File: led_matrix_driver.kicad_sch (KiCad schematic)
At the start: 29 parts, among them J2 Screw_Terminal_01x02, J3 Screw_Terminal_01x02, J4 Conn_01x06_Pin, J5 Conn_02x17_Odd_Even, SW1 CK KMS221GPLFS, SW2 CK KMS221GPLFS, U2 Pico, U3 ESP32-WROOM-32, U4 AP1117-33, U5 74HCT245, U6 Teensy4.0, U7 74HCT245

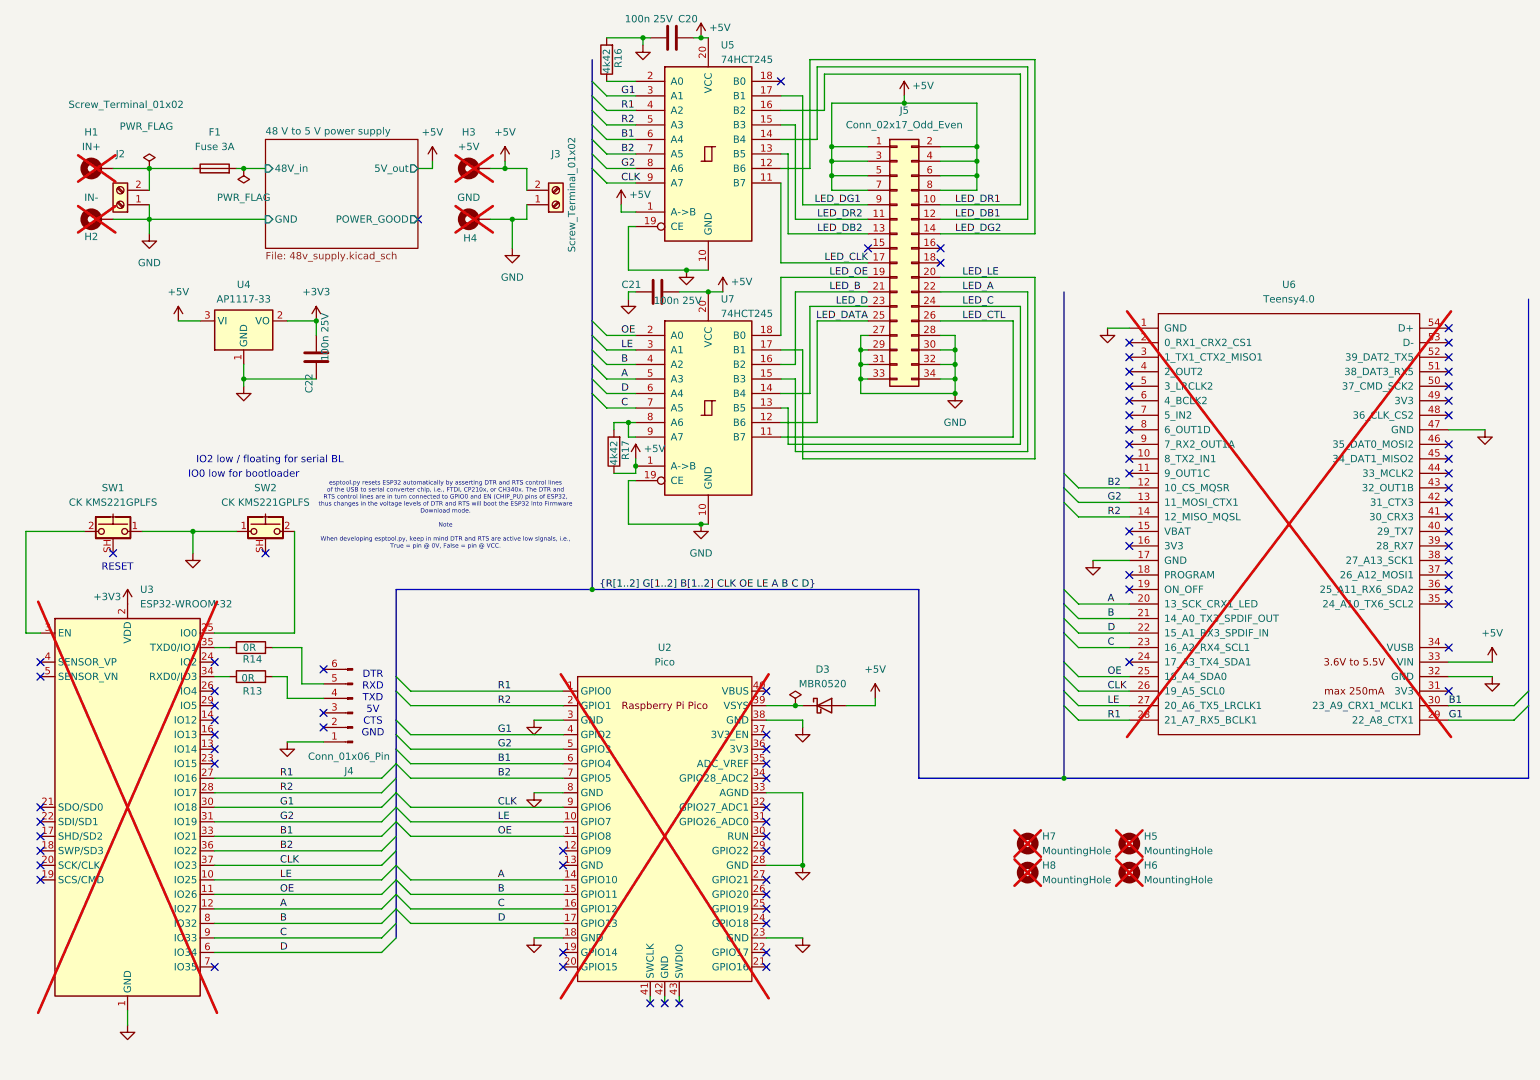
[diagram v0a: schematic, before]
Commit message: Added SPI ESP32-Pico. Last component JLCPCB codes
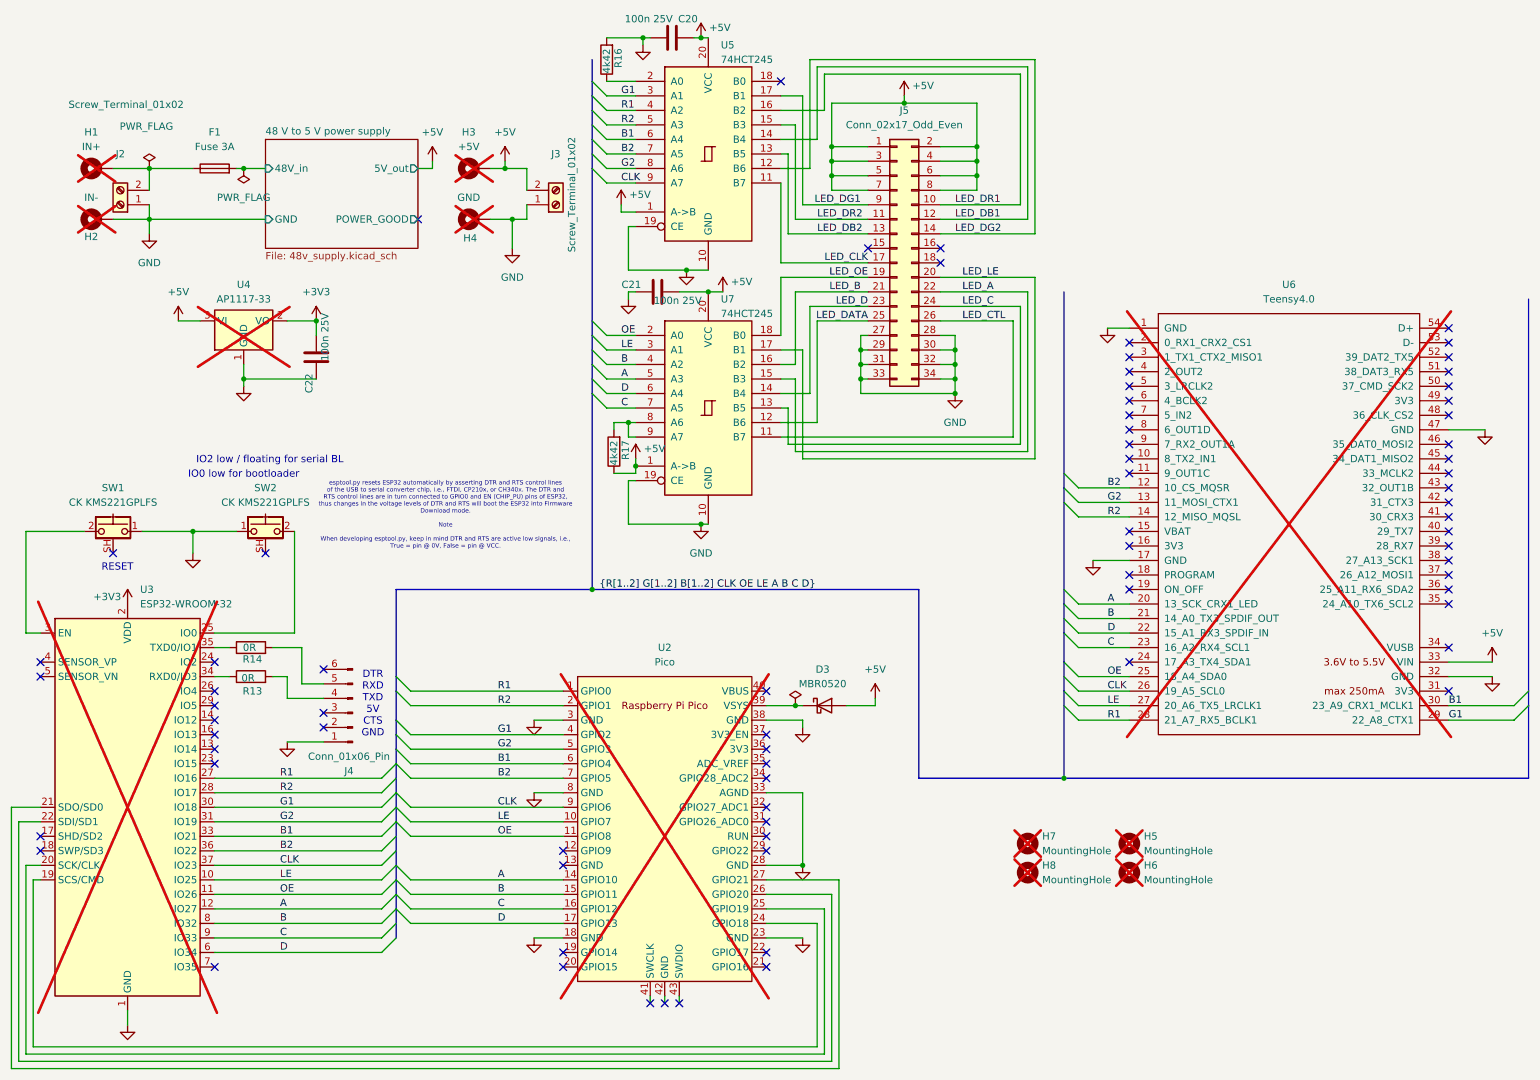
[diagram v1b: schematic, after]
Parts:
- R16, R17: LCSC (none) -> C2933223
- U4: now not fitted
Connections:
- net at U2.24 (GPIO18): now also U3.19 (SCS/CMD)
- net at U2.25 (GPIO19): now also U3.20 (SCK/CLK)
- net at U2.26 (GPIO20): now also U3.22 (SDI/SD1)
- net at U2.27 (GPIO21): now also U3.21 (SDO/SD0)
- no-connect marks 84 -> 76
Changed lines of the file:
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@@
 	)
 	(no_connect
-		(at 144.78 171.45)
-	)
-	(no_connect
 		(at 109.22 176.53)
 	)
@@
 	)
 	(no_connect
-		(at 17.78 163.83)
-	)
-	(no_connect
 		(at 67.31 137.16)
 	)
@@
 	)
 	(no_connect
-		(at 144.78 163.83)
-	)
-	(no_connect
 		(at 48.26 140.97)
 	)
@@
 	)
 	(no_connect
-		(at 17.78 161.29)
-	)
-	(no_connect
 		(at 30.48 106.68)
 	)
@@
 	)
 	(no_connect
-		(at 144.78 168.91)
-	)
-	(no_connect
 		(at 264.16 82.55)
 	)
@@
 	)
 	(no_connect
-		(at 17.78 153.67)
-	)
-	(no_connect
 		(at 129.54 185.42)
 	)
@@
 	)
 	(no_connect
-		(at 144.78 166.37)
-	)
-	(no_connect
 		(at 144.78 156.21)
 	)
@@
 	)
 	(no_connect
-		(at 17.78 151.13)
-	)
-	(no_connect
 		(at 208.28 92.71)
 	)
@@
 	(wire
 		(pts
+			(xy 17.78 153.67) (xy 13.97 153.67)
+		)
+		(stroke
+			(width 0)
+			(type default)
+		)
+	)
+	(wire
+		(pts
 			(xy 168.91 26.67) (xy 168.91 27.94)
 		)
@@
 	(wire
 		(pts
+			(xy 154.94 194.31) (xy 15.24 194.31)
+		)
+		(stroke
+			(width 0)
+			(type default)
+		)
+	)
+	(wire
+		(pts
 			(xy 102.87 45.72) (xy 102.87 48.26)
 		)
@@
 	(wire
 		(pts
+			(xy 154.94 168.91) (xy 154.94 194.31)
+		)
+		(stroke
+			(width 0)
+			(type default)
+		)
+	)
+	(wire
+		(pts
 			(xy 48.26 146.05) (xy 77.47 146.05)
 		)
@@
 	(wire
 		(pts
+			(xy 153.67 171.45) (xy 153.67 193.04)
+		)
+		(stroke
+			(width 0)
+			(type default)
+		)
+	)
+	(wire
+		(pts
 			(xy 175.26 68.58) (xy 177.8 68.58)
 		)
@@
 		)
 	)
+	(wire
+		(pts
+			(xy 144.78 171.45) (xy 153.67 171.45)
+		)
+		(stroke
+			(width 0)
+			(type default)
+		)
+	)
 	(bus
 		(pts
@@
 	(wire
 		(pts
+			(xy 12.7 196.85) (xy 12.7 151.13)
+		)
+		(stroke
+			(width 0)
+			(type default)
+		)
+	)
+	(wire
+		(pts
 			(xy 66.04 66.04) (xy 66.04 68.58)
 		)
@@
 	(wire
 		(pts
+			(xy 16.51 163.83) (xy 16.51 193.04)
+		)
+		(stroke
+			(width 0)
+			(type default)
+		)
+	)
+	(wire
+		(pts
 			(xy 151.13 148.59) (xy 151.13 161.29)
 		)
@@
 	(wire
 		(pts
+			(xy 17.78 163.83) (xy 16.51 163.83)
+		)
+		(stroke
+			(width 0)
+			(type default)
+		)
+	)
+	(wire
+		(pts
 			(xy 118.11 83.82) (xy 118.11 85.09)
 		)
@@
 	(wire
 		(pts
+			(xy 13.97 153.67) (xy 13.97 195.58)
+		)
+		(stroke
+			(width 0)
+			(type default)
+		)
+	)
+	(wire
+		(pts
 			(xy 30.48 48.26) (xy 36.83 48.26)
 		)
@@
 	(wire
 		(pts
+			(xy 144.78 168.91) (xy 154.94 168.91)
+		)
+		(stroke
+			(width 0)
+			(type default)
+		)
+	)
+	(wire
+		(pts
 			(xy 151.13 26.67) (xy 151.13 45.72)
 		)
@@
 	(wire
 		(pts
+			(xy 15.24 161.29) (xy 17.78 161.29)
+		)
+		(stroke
+			(width 0)
+			(type default)
+		)
+	)
+	(wire
+		(pts
 			(xy 156.21 35.56) (xy 162.56 35.56)
 		)
@@
 	(wire
 		(pts
+			(xy 15.24 194.31) (xy 15.24 161.29)
+		)
+		(stroke
+			(width 0)
+			(type default)
+		)
+	)
+	(wire
+		(pts
 			(xy 181.61 35.56) (xy 181.61 38.1)
 		)
@@
 	(wire
 		(pts
+			(xy 157.48 196.85) (xy 12.7 196.85)
+		)
+		(stroke
+			(width 0)
+			(type default)
+		)
+	)
+	(wire
+		(pts
 			(xy 199.39 95.25) (xy 208.28 95.25)
 		)
@@
 	(wire
 		(pts
+			(xy 13.97 195.58) (xy 156.21 195.58)
+		)
+		(stroke
+			(width 0)
+			(type default)
+		)
+	)
+	(wire
+		(pts
 			(xy 82.55 156.21) (xy 109.22 156.21)
 		)
@@
 	(wire
 		(pts
+			(xy 16.51 193.04) (xy 153.67 193.04)
+		)
+		(stroke
+			(width 0)
+			(type default)
+		)
+	)
+	(wire
+		(pts
 			(xy 82.55 138.43) (xy 109.22 138.43)
 		)
@@
 		)
 	)
+	(wire
+		(pts
+			(xy 12.7 151.13) (xy 17.78 151.13)
+		)
+		(stroke
+			(width 0)
+			(type default)
+		)
+	)
 	(bus
 		(pts
@@
 	(wire
 		(pts
+			(xy 144.78 163.83) (xy 157.48 163.83)
+		)
+		(stroke
+			(width 0)
+			(type default)
+		)
+	)
+	(wire
+		(pts
 			(xy 199.39 130.81) (xy 208.28 130.81)
 		)
@@
 	(wire
 		(pts
+			(xy 144.78 166.37) (xy 156.21 166.37)
+		)
+		(stroke
+			(width 0)
+			(type default)
+		)
+	)
+	(wire
+		(pts
 			(xy 199.39 120.65) (xy 208.28 120.65)
 		)
@@
 	(wire
 		(pts
+			(xy 157.48 163.83) (xy 157.48 196.85)
+		)
+		(stroke
+			(width 0)
+			(type default)
+		)
+	)
+	(wire
+		(pts
 			(xy 144.78 173.99) (xy 151.13 173.99)
 		)
@@
 	(wire
 		(pts
+			(xy 156.21 166.37) (xy 156.21 195.58)
+		)
+		(stroke
+			(width 0)
+			(type default)
+		)
+	)
+	(wire
+		(pts
 			(xy 53.34 39.37) (xy 57.15 39.37)
 		)
@@
 		(in_bom yes)
 		(on_board yes)
-		(dnp no)
+		(dnp yes)
 		(fields_autoplaced yes)
 		(property "Reference" "U4"
@@
 			)
 		)
-		(property "LCSC" ""
+		(property "LCSC" "C2933223"
 			(at 116.84 20.32 0)
 			(effects
@@
 			)
 		)
-		(property "LCSC" ""
+		(property "LCSC" "C2933223"
 			(at 118.11 88.9 0)
 			(effects

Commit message: Corrected HCT245 JLCPCB code. Resulted in HCT244, now HCT245
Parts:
- U5, U7: LCSC C6776 -> C94773
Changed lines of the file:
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@@
 			)
 		)
-		(property "LCSC" "C6776"
+		(property "LCSC" "C94773"
 			(at 134.62 36.83 0)
 			(effects
@@
 			)
 		)
-		(property "LCSC" "C6776"
+		(property "LCSC" "C94773"
 			(at 134.62 81.28 0)
 			(effects

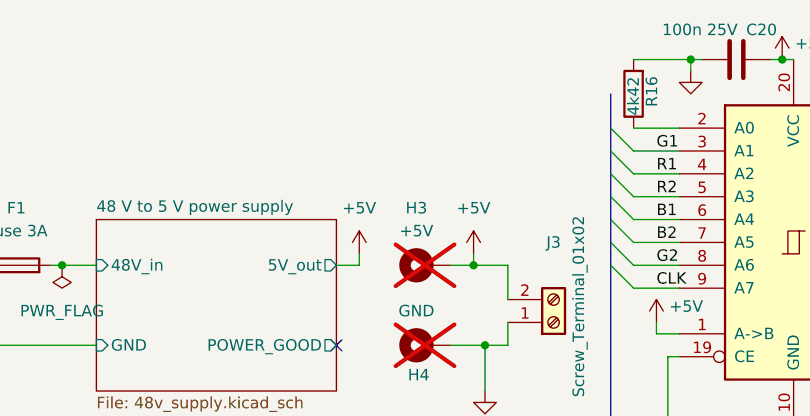
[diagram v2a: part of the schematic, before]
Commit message: Added comment about 5V direct supply
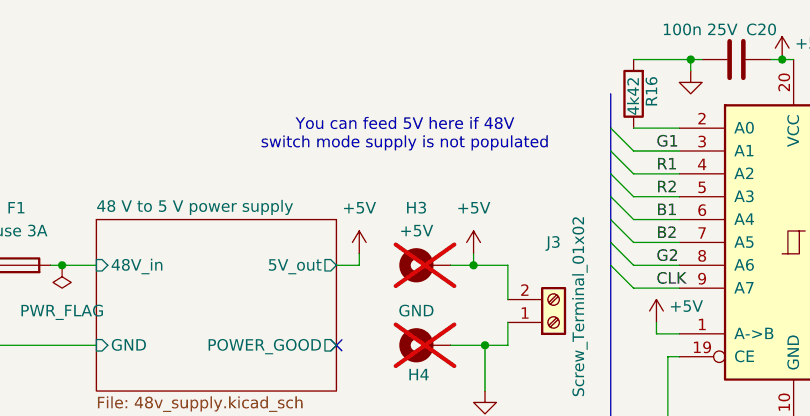
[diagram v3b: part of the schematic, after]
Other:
- note added: "You can feed 5V here if 48V switch mode supply is not populated"
